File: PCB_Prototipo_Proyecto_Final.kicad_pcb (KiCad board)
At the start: 2 copper layers, 165.1 x 154.9 mm, 151 parts, among them IC1 UA741CP, J1 VIN, J10 Terminal_Sensores_Nivel, J11 Terminal_Sensor_Flujo, J12 Rele_4, J13 Rele_7, J14 Rele_1, J15 Rele_5, J16 Rele_2, J17 Rele_3, J18 Rele_6, J19 Pin GND, J2 Conn_01x15, J20 Conector 3V3, J21 Conector GND, J22 Pin_3V3, J23 Pin_3V3, J24 Pin GND, J25 Pin_3V3, J26 Pin GND, J27 Pin_3V3, J28 Pin_3V3, J29 Pin_3V3, J3 Conn_01x15, J30 Pin GND, J31 Pin GND, J32 Pin GND, J33 Pin GND, J34 Pin GND, J35 Pin GND, J36 Pin GND, J37 Pin GND, J38 Pin GND, J39 Pin GND, J4 Terminal_Sensor_pH, J40 Pin GND, J41 Pin GND, J42 Pin GND, J43 Conector GND, J5 Terminal_Sensor_CO2, J6 Terminal_Sensor_TDS, J7 Terminal_Sensor_Temp_Sumerg, J8 Terminal_Sensor_Iluminacion, J9 Terminal_Sensor_Temp_y_Hum, K1 SRD-05VDC-SL-C, K2 SRD-05VDC-SL-C, K3 SRD-05VDC-SL-C, K4 SRD-05VDC-SL-C, K5 SRD-05VDC-SL-C, K6 SRD-05VDC-SL-C, K7 SRD-05VDC-SL-C, Q1 2N7002, Q10 PMBT3904,235, Q11 PMBT3904,235, Q12 PMBT3904,235, Q13 PMBT3904,235, Q14 PMBT3904,235, Q15 PMBT3904,235, Q2 2N7002, Q3 2N7002, Q4 2N7002, Q5 2N7002, Q6 2N7002, Q7 2N7002, Q8 2N7002, Q9 PMBT3904,235, U1 LM2596S-5, U2 LM1117-3.3, U3 MCP23008-xP

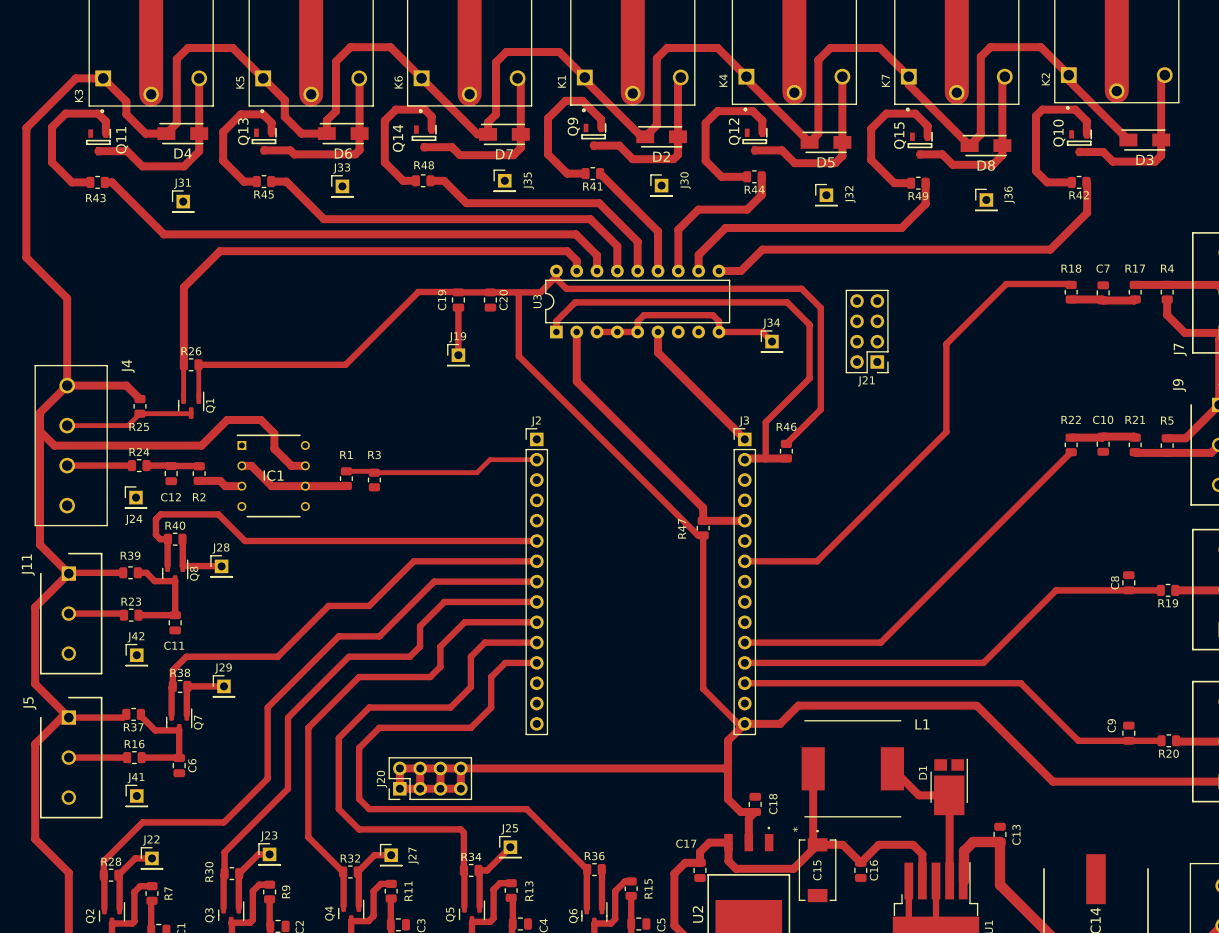
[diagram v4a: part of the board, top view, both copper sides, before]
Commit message: Modificación de componentes.
Se agregó al PCB los footprints de los componentes que se cambiaron según la disponibilidad que había (resistencias, transistor de los relés, diodo de los reles)
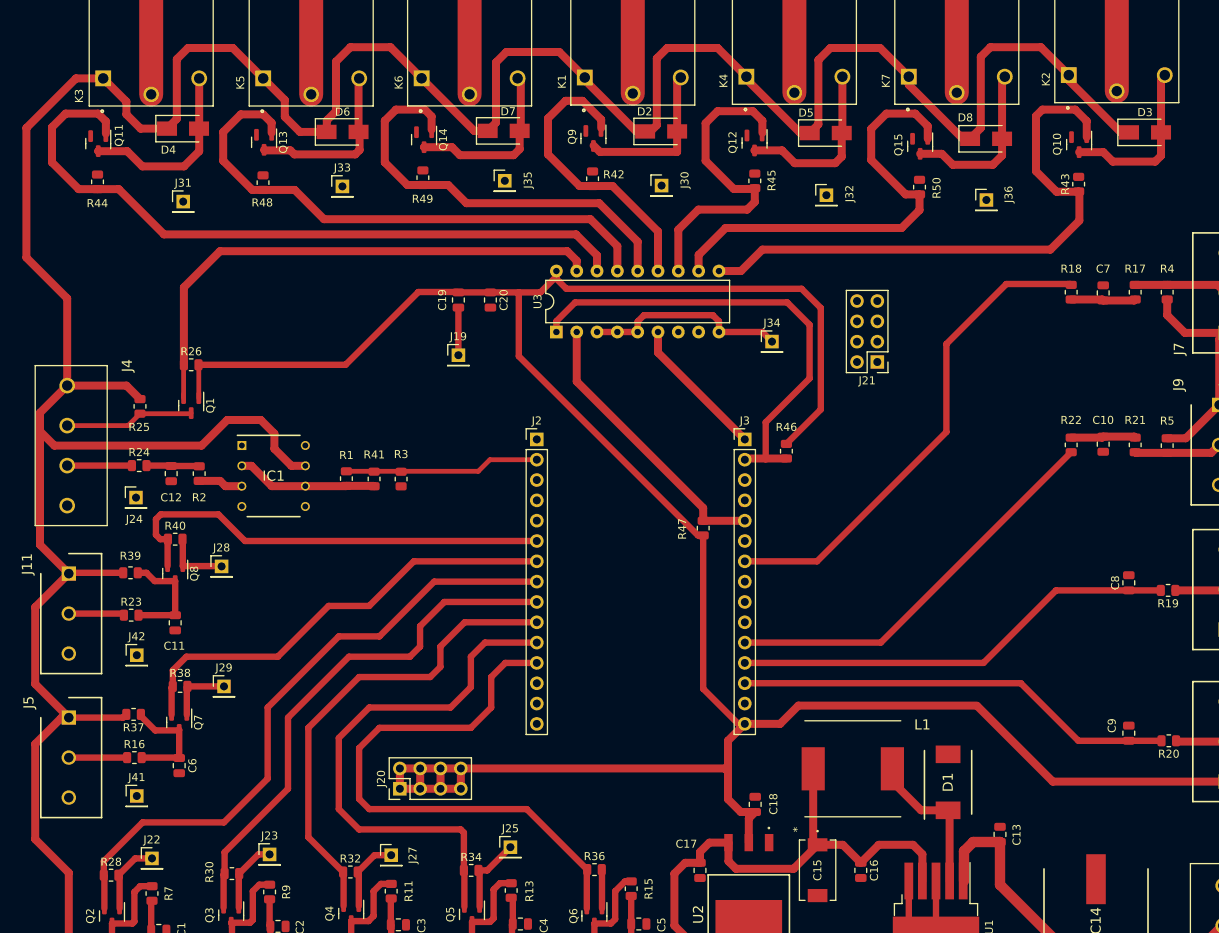
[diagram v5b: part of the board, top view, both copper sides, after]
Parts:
- added R50: 10K, 1/8W, Resistor_SMD:R_0805_2012Metric, F.Cu at (254.2, 95.0)
- C15: value 220 uF, 10V -> 470 uF, 50V
- C17, C18, C19: value 10 uF, 10V -> 10 uF, 50V
- D1: value PMEG060V050EPD -> B340-13-F; footprint Package_TO_SOT_SMD:Nexperia_CFP15_SOT-1289 -> B340-13-F:DIOM7959X250N
- D2, D3, D4, D5, D6, D7, D8: value FM4003-W -> M7; footprint FM4003W:DIOM5025X231N -> Diode_SMD:D_SMA
- Q10, Q11, Q12, Q13, Q14, Q15, Q9: value PMBT3904,235 -> 2N7002; footprint PMBT3904,235:SOT95P230X110-3N -> Package_TO_SOT_SMD:SOT-23
- R1: value 549, 1/4W -> 10K, 1/8W
- R10, R11, R12, R13, R14, R15, R16, R17, R18, R19, R20, R21, R22, R23, R24, R6, R7, R8, R9: value 27, 1/2W -> 50, 1/8W
- R2: value 1K, 1/2W -> 1,5K, 1/8W
- R25, R26, R27, R28, R29, R30, R31, R32, R33, R34, R35, R36, R37, R38, R39, R40: value 10K, 1/2W -> 10K, 1/8W
- R3: value 1K, 1/2W -> 10K, 1/8W
- R4, R5: value 4,7K, 1/2W -> 4,7K, 1/8W
- R41, R42, R43, R44, R45, R48, R49: value 820, 1/2W -> 10K, 1/8W
- R46, R47: value 4.7K, 1/2W -> 4.7K, 1/8W
- moved R43 122.6 mm to (274.1, 94.6), turned to 90 degrees
- moved R44 82.1 mm to (151.4, 94.3), turned to 90 degrees
- moved R49 61.9 mm to (192.1, 93.8), turned to 90 degrees
- moved R45 61.4 mm to (233.6, 94.2), turned to 90 degrees
- moved R42 60.8 mm to (213.3, 93.9), turned to 90 degrees
- moved R41 47.0 mm to (186.0, 131.4), turned to 90 degrees
- moved R48 20.0 mm to (172.1, 94.4), turned to 90 degrees
- moved R3 3.34 mm to (189.4, 131.5)
- moved D5 1.17 mm to (242.5, 88.2)
- moved D3 0.95 mm to (282.4, 88.1)
- moved D8 0.85 mm to (262.5, 88.9)
- moved D2 0.67 mm to (221.9, 88.0)
- moved D1 0.63 mm to (257.8, 169.4)
- moved D4 0.62 mm to (162.1, 87.7)
- moved D7 0.45 mm to (202.2, 87.9)
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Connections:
- D1 pad 1: GND -> Net-(D1-Pad1)
- L1 pad 1: Net-(D1-Pad3) -> Net-(D1-Pad1)
- Q10 pad 1: Net-(Q10-Pad1) -> /Microcontrolador/Rele_7
- Q11 pad 1: Net-(Q11-Pad1) -> /Microcontrolador/Rele_1
- Q12 pad 1: Net-(Q12-Pad1) -> /Microcontrolador/Rele_5
- Q13 pad 1: Net-(Q13-Pad1) -> /Microcontrolador/Rele_2
- Q14 pad 1: Net-(Q14-Pad1) -> /Microcontrolador/Rele_3
- Q15 pad 1: Net-(Q15-Pad1) -> /Microcontrolador/Rele_6
- Q9 pad 1: Net-(Q9-Pad1) -> /Microcontrolador/Rele_4
- R41 pad 1: /Microcontrolador/Rele_4 -> Net-(IC1-Pad2)
- R41 pad 2: Net-(Q9-Pad1) -> /Entradas/pH_Analog
- R42 pad 1: /Microcontrolador/Rele_7 -> /Microcontrolador/Rele_4
- R42 pad 2: Net-(Q10-Pad1) -> GND
- R43 pad 1: /Microcontrolador/Rele_1 -> /Microcontrolador/Rele_7
- R43 pad 2: Net-(Q11-Pad1) -> GND
- R44 pad 1: /Microcontrolador/Rele_5 -> /Microcontrolador/Rele_1
- R44 pad 2: Net-(Q12-Pad1) -> GND
- R45 pad 1: /Microcontrolador/Rele_2 -> /Microcontrolador/Rele_5
- R45 pad 2: Net-(Q13-Pad1) -> GND
- R48 pad 1: /Microcontrolador/Rele_3 -> /Microcontrolador/Rele_2
- R48 pad 2: Net-(Q14-Pad1) -> GND
- R49 pad 1: /Microcontrolador/Rele_6 -> /Microcontrolador/Rele_3
- R49 pad 2: Net-(Q15-Pad1) -> GND
- U1 pad 2: Net-(D1-Pad3) -> Net-(D1-Pad1)
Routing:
- net /Microcontrolador/Rele_4: track 15.2 -> 36.8 mm
- net /Microcontrolador/Rele_1: track 67.2 -> 88.7 mm
- net /Microcontrolador/Rele_7: track 52.9 -> 73.9 mm
- net Net-(Q10-Pad1): track 20.9 -> 0.00 mm
- net Net-(Q12-Pad1): track 20.4 -> 0.00 mm
- net /Microcontrolador/Rele_3: track 32.7 -> 53.0 mm
- net /Microcontrolador/Rele_5: track 19.7 -> 40.0 mm
- net /Microcontrolador/Rele_6: track 35.6 -> 55.7 mm
- net Net-(Q15-Pad1): track 19.9 -> 0.00 mm
- net Net-(Q9-Pad1): track 19.8 -> 0.00 mm
- net Net-(Q11-Pad1): track 19.6 -> 0.00 mm
- net /Microcontrolador/Rele_2: track 49.7 -> 69.0 mm
- net Net-(D1-Pad3): track 19.2 -> 0.00 mm
- net Net-(D1-Pad1): track 0.00 -> 19.0 mm
- net Net-(Q14-Pad1): track 18.5 -> 0.00 mm
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
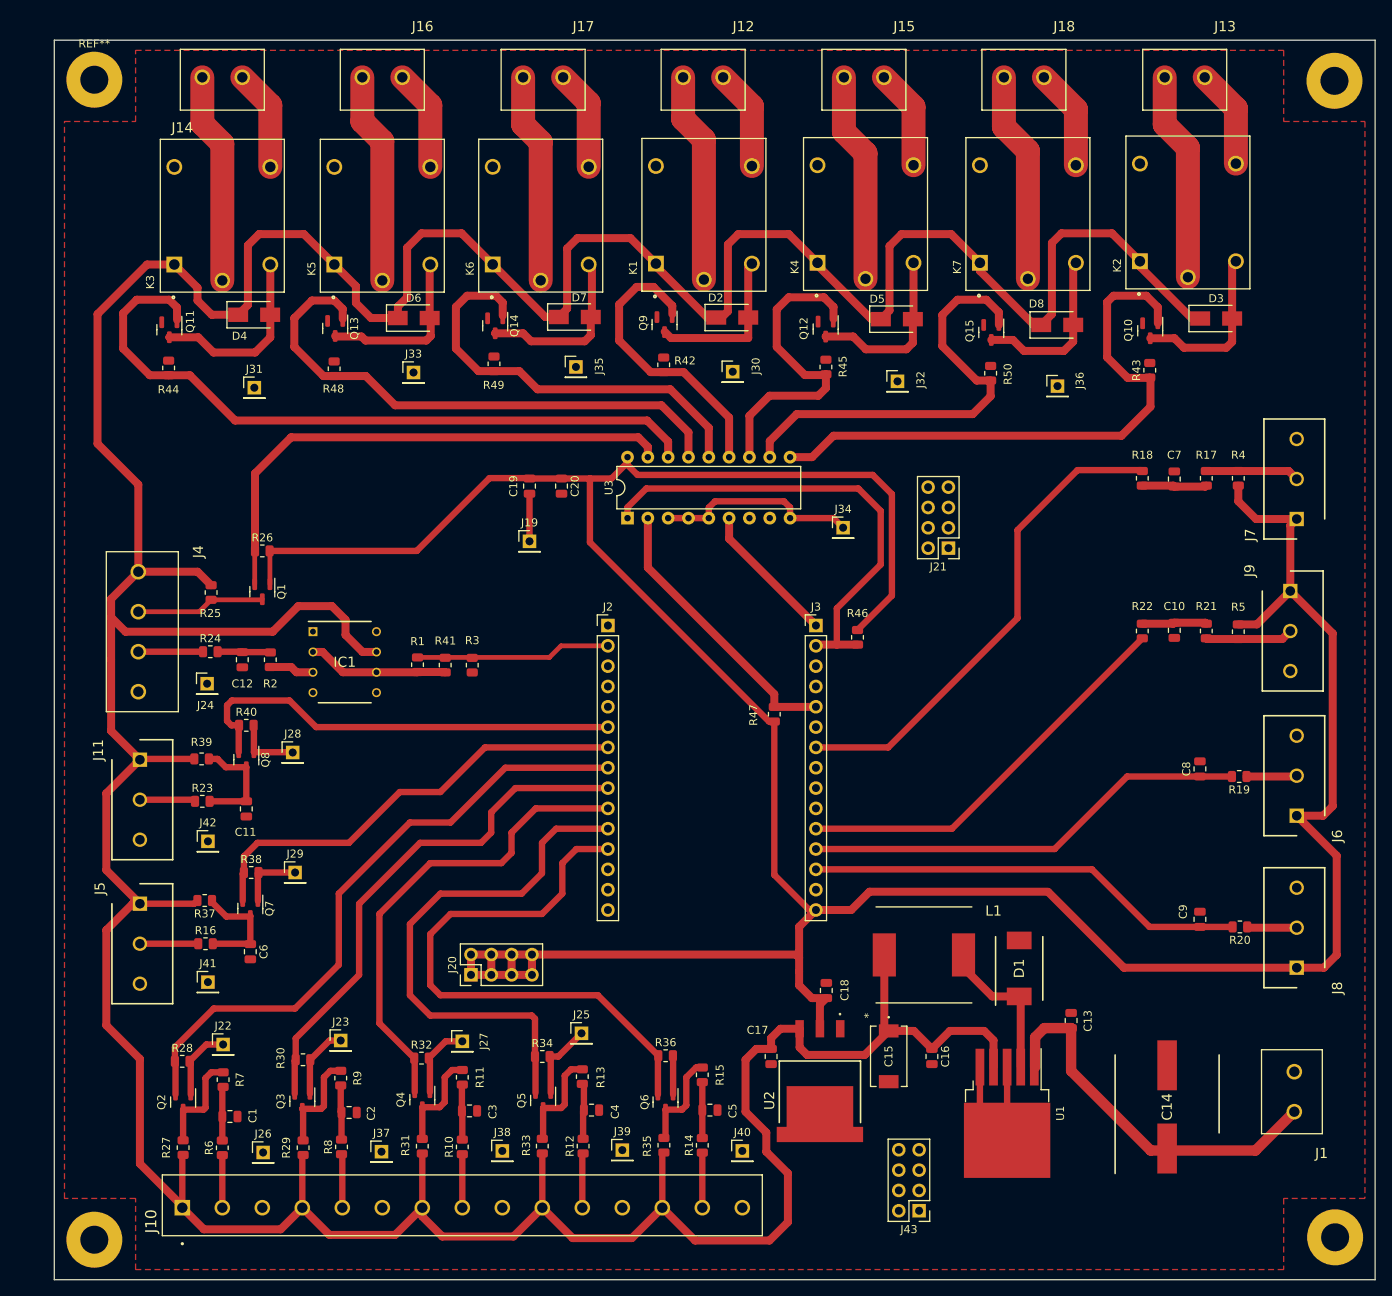
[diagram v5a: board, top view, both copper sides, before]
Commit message: Se cambiaron todos los componentes a la capa BOTTOM.
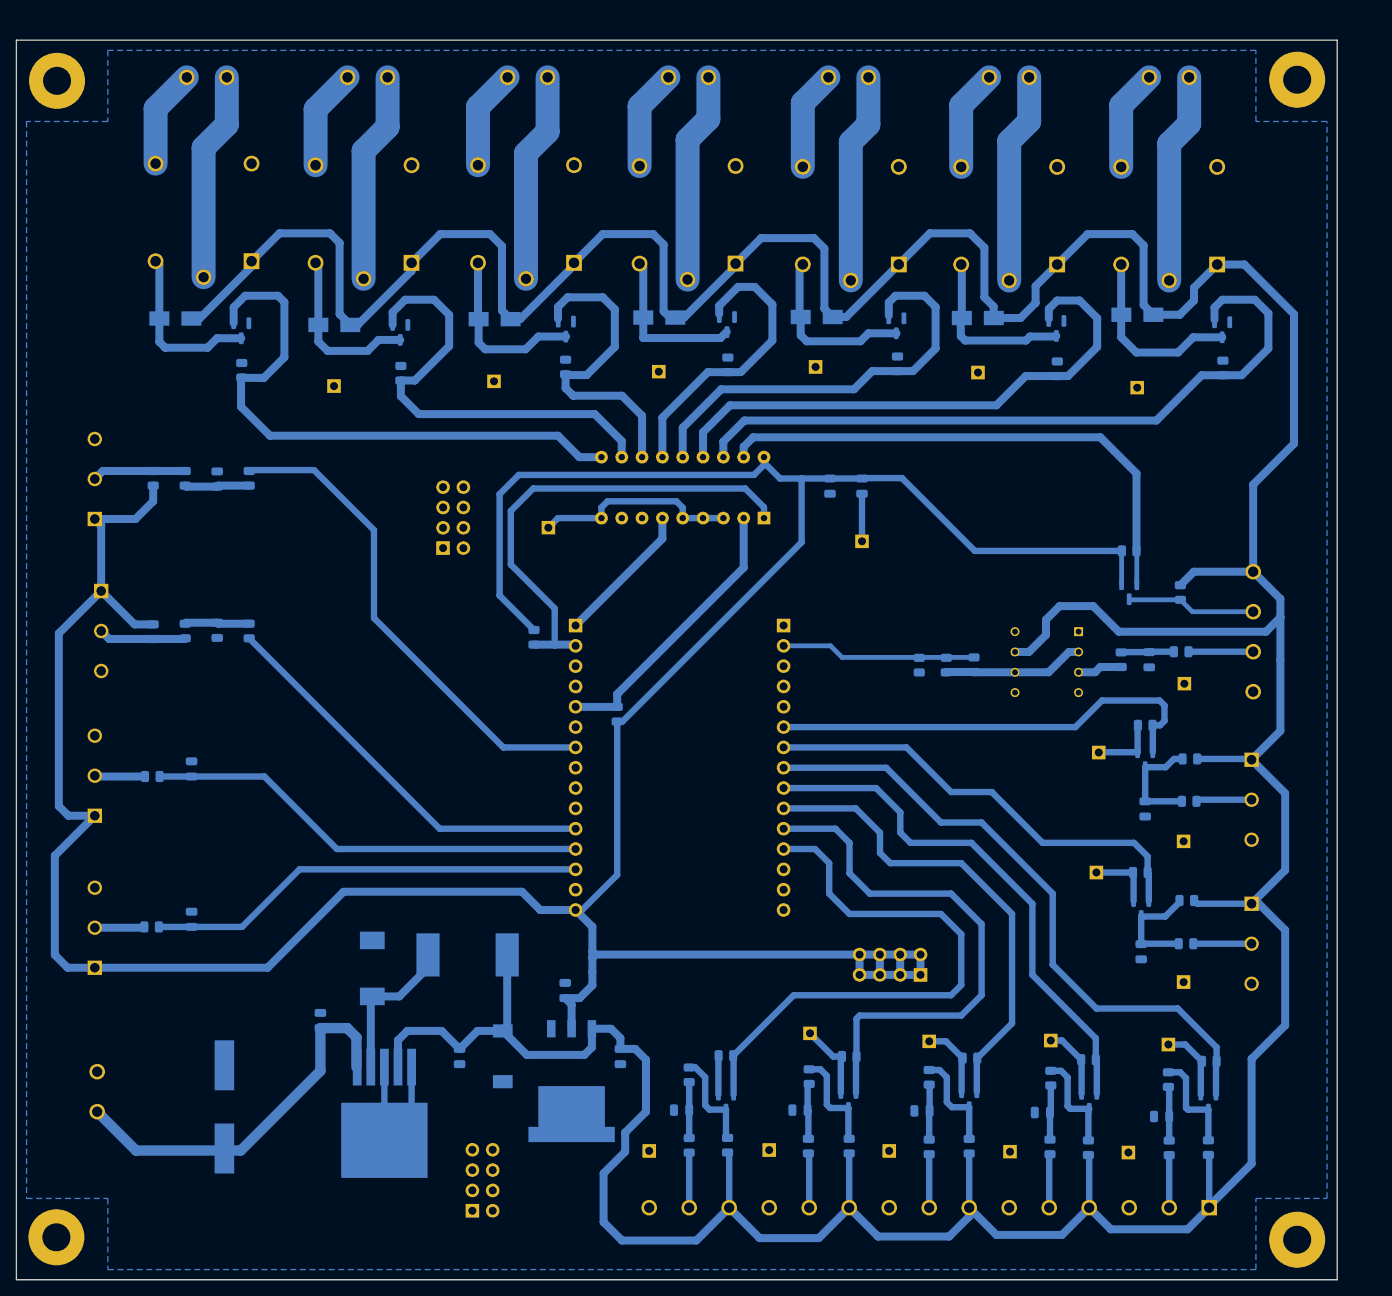
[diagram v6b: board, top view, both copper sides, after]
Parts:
- ? (x3), C1, C10, C11, C12, C13, C14, C15, C16, C17, C18, C19, C2, C20, C3, C4, C5, C6, C7, C8, C9, D1, D2, D3, D4, D5, D6, D7, D8, IC1, J1, J10, J11, J12, J13, J14, J15, J16, J17, J18, J19, J2, J20, J21, J22, J23, J24, J25, J26, J27, J28, J29, J3, J30, J31, J32, J33, J34, J35, J36, J37, J38, J39, J4, J40, J41, J42, J43, J5, J6, J7, J8, J9, K1, K2, K3, K4, K5, K6, K7, L1, Q1, Q10, Q11, Q12, Q13, Q14, Q15, Q2, Q3, Q4, Q5, Q6, Q7, Q8, Q9, R1, R10, R11, R12, R13, R14, R15, R16, R17, R18, R19, R2, R20, R21, R22, R23, R24, R25, R26, R27, R28, R29, R3, R30, R31, R32, R33, R34, R35, R36, R37, R38, R39, R4, R40, R41, R42, R43, R44, R45, R46, R47, R48, R49, R5, R50, R6, R7, R8, R9, REF**, U1, U2, U3: moved to B.Cu
- moved ? 159.8 mm to (137.4, 203.0), turned to 180 degrees
- moved ? 159.7 mm to (137.5, 58.4), turned to 180 degrees
- moved ? 150.4 mm to (292.5, 203.3), turned to 180 degrees
- moved REF** 150.4 mm to (292.5, 58.3), turned to 180 degrees
- moved J6 150.2 mm to (142.2, 150.3)
- moved J7 150.2 mm to (142.2, 113.2)
- moved J8 150.2 mm to (142.2, 169.3)
- moved J1 149.6 mm to (142.5, 187.3)
- moved J9 148.6 mm to (143.0, 122.2)
- moved J4 139.4 mm to (287.0, 119.8)
- moved J11 139.0 mm to (286.8, 143.3)
- moved J5 139.0 mm to (286.8, 161.3)
- moved R20 136.0 mm to (149.3, 164.2), turned to 0 degrees
- moved R19 135.9 mm to (149.4, 145.4), turned to 0 degrees
- moved R4 135.6 mm to (149.5, 108.1)
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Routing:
- added copper zone on B.Cu, net GND
- removed copper zone on F.Cu, net GND
